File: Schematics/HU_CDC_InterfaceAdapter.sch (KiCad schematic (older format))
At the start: 5 parts, among them Q2 2N7000, Q4 2N7000

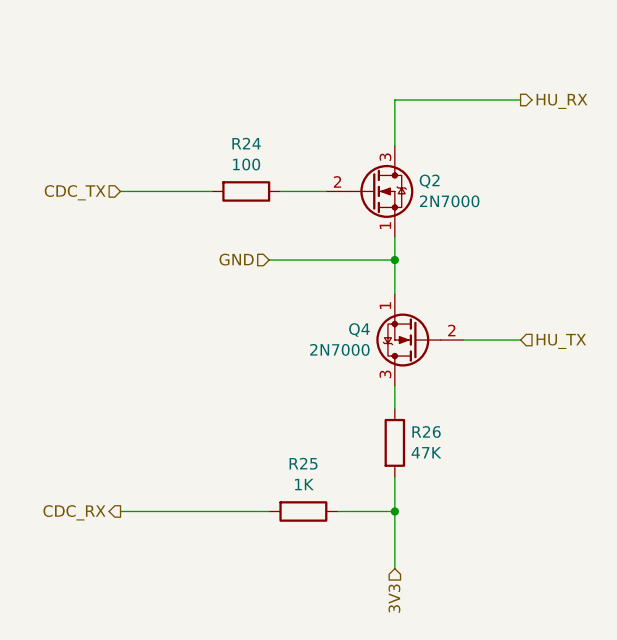
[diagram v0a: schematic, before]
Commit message: Fixed CDC interface schematic; Fixed SPDIF output interface schematic; Added screw terminals; Modified PCB design
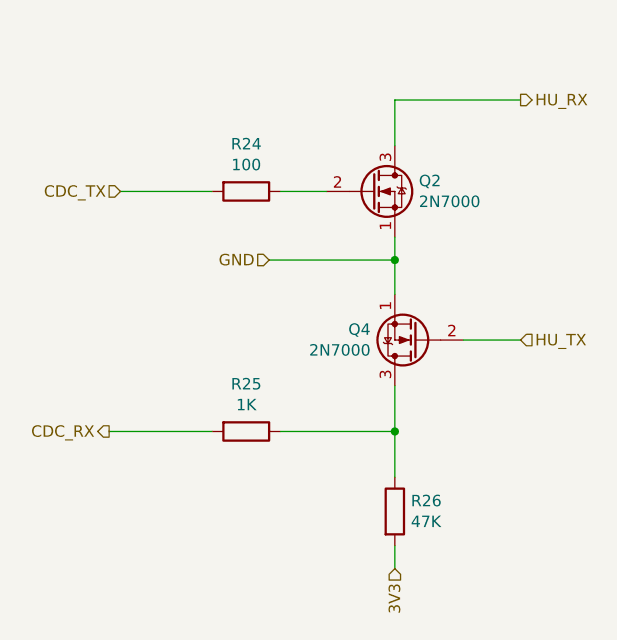
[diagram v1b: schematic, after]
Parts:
- Q2, Q4: footprint Package_TO_SOT_THT:TO-92_Inline -> Package_TO_SOT_THT:TO-92_Inline_Wide
- R24: footprint Resistor_THT:R_Axial_DIN0207_L6.3mm_D2.5mm_P10.16mm_Horizontal -> Resistor_THT:R_Axial_DIN0207_L6.3mm_D2.5mm_P7.62mm_Horizontal
- R25: footprint Resistor_THT:R_Axial_DIN0207_L6.3mm_D2.5mm_P10.16mm_Horizontal -> Resistor_THT:R_Axial_DIN0204_L3.6mm_D1.6mm_P2.54mm_Vertical
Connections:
- net 3V3: no longer R25.1
- net at Q4.3 (D), R26.1: now also R25.1
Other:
- moved on the sheet: R25, R26
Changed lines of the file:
@@
 F 0 "Q2" H 4305 2796 50  0000 L CNN
 F 1 "2N7000" H 4305 2705 50  0000 L CNN
-F 2 "Package_TO_SOT_THT:TO-92_Inline" H 4300 2675 50  0001 L CIN
+F 2 "Package_TO_SOT_THT:TO-92_Inline_Wide" H 4300 2675 50  0001 L CIN
 F 3 "https://www.fairchildsemi.com/datasheets/2N/2N7000.pdf" H 4100 2750 50  0001 L CNN
 	1    4100 2750
@@
 F 0 "Q4" H 4506 3354 50  0000 L CNN
 F 1 "2N7000" H 4506 3445 50  0000 L CNN
-F 2 "Package_TO_SOT_THT:TO-92_Inline" H 4500 3325 50  0001 L CIN
+F 2 "Package_TO_SOT_THT:TO-92_Inline_Wide" H 4500 3325 50  0001 L CIN
 F 3 "https://www.fairchildsemi.com/datasheets/2N/2N7000.pdf" H 4300 3400 50  0001 L CNN
 	1    4300 3400
@@
 F 0 "R24" V 3343 2750 50  0000 C CNN
 F 1 "100" V 3434 2750 50  0000 C CNN
-F 2 "Resistor_THT:R_Axial_DIN0207_L6.3mm_D2.5mm_P10.16mm_Horizontal" V 3480 2750 50  0001 C CNN
+F 2 "Resistor_THT:R_Axial_DIN0207_L6.3mm_D2.5mm_P7.62mm_Horizontal" V 3480 2750 50  0001 C CNN
 F 3 "~" H 3550 2750 50  0001 C CNN
 	1    3550 2750
@@
 L Device:R R25
 U 1 1 5D1137C8
-P 3800 4150
-F 0 "R25" V 3593 4150 50  0000 C CNN
-F 1 "1K" V 3684 4150 50  0000 C CNN
-F 2 "Resistor_THT:R_Axial_DIN0207_L6.3mm_D2.5mm_P10.16mm_Horizontal" V 3730 4150 50  0001 C CNN
-F 3 "~" H 3800 4150 50  0001 C CNN
-	1    3800 4150
+P 3550 3800
+F 0 "R25" V 3343 3800 50  0000 C CNN
+F 1 "1K" V 3434 3800 50  0000 C CNN
+F 2 "Resistor_THT:R_Axial_DIN0204_L3.6mm_D1.6mm_P2.54mm_Vertical" V 3480 3800 50  0001 C CNN
+F 3 "~" H 3550 3800 50  0001 C CNN
+	1    3550 3800
 	0    1    1    0
 $EndComp
@@
 L Device:R R26
 U 1 1 5D11384C
-P 4200 3850
-F 0 "R26" H 4270 3896 50  0000 L CNN
-F 1 "47K" H 4270 3805 50  0000 L CNN
-F 2 "Resistor_THT:R_Axial_DIN0207_L6.3mm_D2.5mm_P10.16mm_Horizontal" V 4130 3850 50  0001 C CNN
-F 3 "~" H 4200 3850 50  0001 C CNN
-	1    4200 3850
+P 4200 4150
+F 0 "R26" H 4270 4196 50  0000 L CNN
+F 1 "47K" H 4270 4105 50  0000 L CNN
+F 2 "Resistor_THT:R_Axial_DIN0207_L6.3mm_D2.5mm_P10.16mm_Horizontal" V 4130 4150 50  0001 C CNN
+F 3 "~" H 4200 4150 50  0001 C CNN
+	1    4200 4150
 	1    0    0    -1
 $EndComp
@@
 Text HLabel 4750 3400 2    50   Input ~ 0
 HU_TX
-Text HLabel 3000 4150 0    50   Output ~ 0
+Text HLabel 2950 3800 0    50   Output ~ 0
 CDC_RX
 Wire Wire Line
-	3000 4150 3650 4150
+	2950 3800 3400 3800
 Text HLabel 4200 4400 3    50   Input ~ 0
 3V3
@@
 	4750 3400 4500 3400
 Wire Wire Line
-	3950 4150 4200 4150
+	4200 4000 4200 3800
 Wire Wire Line
-	4200 4150 4200 4000
+	4200 4300 4200 4400
 Wire Wire Line
-	4200 3700 4200 3600
+	3700 3800 4200 3800
+Connection ~ 4200 3800
 Wire Wire Line
-	4200 4400 4200 4150
-Connection ~ 4200 4150
+	4200 3800 4200 3600
 $EndSCHEMATC

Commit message: Fixed voltage level issues between BT module and WM8804; fixed CDC Emulator hw interface; modified PCB design
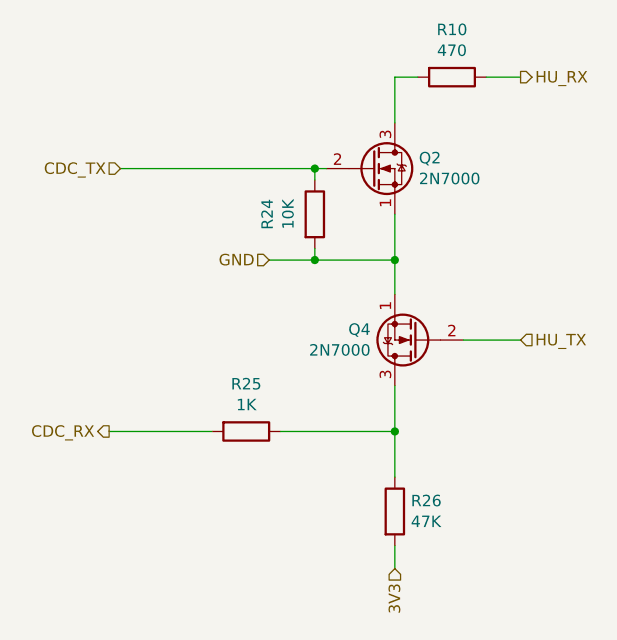
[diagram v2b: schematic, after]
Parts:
- added R10: 470, Resistor_THT:R_Axial_DIN0204_L3.6mm_D1.6mm_P2.54mm_Vertical, symbol Device:R
- R24: value 100 -> 10K; footprint Resistor_THT:R_Axial_DIN0207_L6.3mm_D2.5mm_P7.62mm_Horizontal -> Resistor_THT:R_Axial_DIN0204_L3.6mm_D1.6mm_P2.54mm_Vertical
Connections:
- net CDC_TX: now also Q2.2 (G), R24.1; no longer R24.2
- net GND: now also R24.2
- net HU_RX: now also R10.1; no longer Q2.3 (D)
- new net: Q2.3 (D), R10.2
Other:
- moved on the sheet: Q2, R24
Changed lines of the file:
@@
 $Descr A4 11693 8268
 encoding utf-8
-Sheet 8 8
+Sheet 7 7
 Title ""
 Date ""
@@
 L Transistor_FET:2N7000 Q2
 U 1 1 5D113680
-P 4100 2750
-F 0 "Q2" H 4305 2796 50  0000 L CNN
-F 1 "2N7000" H 4305 2705 50  0000 L CNN
-F 2 "Package_TO_SOT_THT:TO-92_Inline_Wide" H 4300 2675 50  0001 L CIN
-F 3 "https://www.fairchildsemi.com/datasheets/2N/2N7000.pdf" H 4100 2750 50  0001 L CNN
-	1    4100 2750
+P 4100 2650
+F 0 "Q2" H 4305 2696 50  0000 L CNN
+F 1 "2N7000" H 4305 2605 50  0000 L CNN
+F 2 "Package_TO_SOT_THT:TO-92_Inline_Wide" H 4300 2575 50  0001 L CIN
+F 3 "https://www.fairchildsemi.com/datasheets/2N/2N7000.pdf" H 4100 2650 50  0001 L CNN
+	1    4100 2650
 	1    0    0    -1
 $EndComp
@@
 L Device:R R24
 U 1 1 5D11378B
-P 3550 2750
-F 0 "R24" V 3343 2750 50  0000 C CNN
-F 1 "100" V 3434 2750 50  0000 C CNN
-F 2 "Resistor_THT:R_Axial_DIN0207_L6.3mm_D2.5mm_P7.62mm_Horizontal" V 3480 2750 50  0001 C CNN
-F 3 "~" H 3550 2750 50  0001 C CNN
-	1    3550 2750
-	0    1    1    0
+P 3850 2850
+F 0 "R24" V 3643 2850 50  0000 C CNN
+F 1 "10K" V 3734 2850 50  0000 C CNN
+F 2 "Resistor_THT:R_Axial_DIN0204_L3.6mm_D1.6mm_P2.54mm_Vertical" V 3780 2850 50  0001 C CNN
+F 3 "~" H 3850 2850 50  0001 C CNN
+	1    3850 2850
+	1    0    0    -1
 $EndComp
 $Comp
@@
 	1    0    0    -1
 $EndComp
-Wire Wire Line
-	3700 2750 3900 2750
 Text HLabel 3650 3050 0    50   Input ~ 0
 GND
-Wire Wire Line
-	4200 2950 4200 3050
-Wire Wire Line
-	4200 3050 3650 3050
-Text HLabel 3000 2750 0    50   Input ~ 0
+Text HLabel 3000 2650 0    50   Input ~ 0
 CDC_TX
-Wire Wire Line
-	3000 2750 3400 2750
-Text HLabel 4750 2350 2    50   Output ~ 0
+Text HLabel 4750 2250 2    50   Output ~ 0
 HU_RX
 Wire Wire Line
-	4200 2550 4200 2350
-Wire Wire Line
-	4200 2350 4750 2350
-Connection ~ 4200 3050
+	4200 2450 4200 2250
 Text HLabel 4750 3400 2    50   Input ~ 0
 HU_TX
@@
 Wire Wire Line
 	4200 3800 4200 3600
+Connection ~ 3850 2650
+Wire Wire Line
+	3850 2650 3900 2650
+Wire Wire Line
+	3000 2650 3850 2650
+Wire Wire Line
+	3650 3050 3850 3050
+Wire Wire Line
+	3850 2700 3850 2650
+Wire Wire Line
+	3850 3000 3850 3050
+Connection ~ 3850 3050
+Wire Wire Line
+	3850 3050 4200 3050
+Wire Wire Line
+	4200 2850 4200 3050
+Connection ~ 4200 3050
+$Comp
+L Device:R R10
+U 1 1 5DB88B27
+P 4450 2250
+F 0 "R10" V 4243 2250 50  0000 C CNN
+F 1 "470" V 4334 2250 50  0000 C CNN
+F 2 "Resistor_THT:R_Axial_DIN0204_L3.6mm_D1.6mm_P2.54mm_Vertical" V 4380 2250 50  0001 C CNN
+F 3 "~" H 4450 2250 50  0001 C CNN
+	1    4450 2250
+	0    1    1    0
+$EndComp
+Wire Wire Line
+	4300 2250 4200 2250
+Wire Wire Line
+	4600 2250 4750 2250
 $EndSCHEMATC
